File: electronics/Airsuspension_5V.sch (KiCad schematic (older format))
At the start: 5 parts, among them U9 LM2574M-5

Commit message: Some more fottprints added to PCB
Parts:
- C18: footprint (none) -> Capacitors_SMD:c_elec_6.3x7.7
- C19: footprint (none) -> Capacitors_SMD:c_elec_8x10.5
- D12: footprint (none) -> Diodes_SMD:Diode-SMA_Handsoldering
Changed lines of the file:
@@
 F 0 "D12" H 6300 3100 50  0000 C CNN
 F 1 "SS110" H 6300 2900 50  0000 C CNN
-F 2 "" H 6300 3000 60  0001 C CNN
+F 2 "Diodes_SMD:Diode-SMA_Handsoldering" H 6300 3000 60  0001 C CNN
 F 3 "http://www.farnell.com/datasheets/1662144.pdf" H 6300 3000 60  0001 C CNN
 F 4 "4085140" H 6300 3000 60  0001 C CNN "farnell"
@@
 F 0 "C18" H 5950 4000 50  0000 L CNN
 F 1 "47uF lowESR" H 5950 3800 50  0000 L CNN
-F 2 "" H 5938 3750 30  0001 C CNN
+F 2 "Capacitors_SMD:c_elec_6.3x7.7" H 5938 3750 30  0001 C CNN
 F 3 "http://www.farnell.com/datasheets/1679509.pdf" H 5900 3900 60  0001 C CNN
 F 4 "EEETQV470XAP" H 5900 3900 60  0001 C CNN "name"
@@
 F 0 "C19" H 7300 3100 50  0000 L CNN
 F 1 "470uF low esr" H 7000 2900 50  0000 L CNN
-F 2 "" H 7288 2850 30  0001 C CNN
+F 2 "Capacitors_SMD:c_elec_8x10.5" H 7288 2850 30  0001 C CNN
 F 3 "http://www.farnell.com/datasheets/1790597.pdf" H 7250 3000 60  0001 C CNN
 F 4 "EEEFT1E471AP" H 7250 3000 60  0001 C CNN "name"

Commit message: Some more footprints and beginning PCB work
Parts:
- L1: footprint (none) -> kicad_lib:Inductor_MSS1260
- U9: footprint (none) -> kicad_lib:SOIC14_W
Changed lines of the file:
@@
 F 0 "U9" H 5100 3300 60  0000 C CNN
 F 1 "LM2574M-5" H 5100 2500 60  0000 C CNN
-F 2 "" H 5050 2800 60  0001 C CNN
+F 2 "kicad_lib:SOIC14_W" H 5050 2800 60  0001 C CNN
 F 3 "http://www.farnell.com/datasheets/1896110.pdf" H 5050 2800 60  0001 C CNN
 F 4 "9489908" H 5100 2900 60  0001 C CNN "farnell"
@@
 F 0 "L1" V 6550 2800 50  0000 C CNN
 F 1 "470uH" V 6700 2800 50  0000 C CNN
-F 2 "" H 6600 2800 60  0001 C CNN
+F 2 "kicad_lib:Inductor_MSS1260" H 6600 2800 60  0001 C CNN
 F 3 "http://www.farnell.com/datasheets/1681951.pdf" H 6600 2800 60  0001 C CNN
 F 4 "MSS1260-474KLD" V 6600 2800 60  0001 C CNN "name"

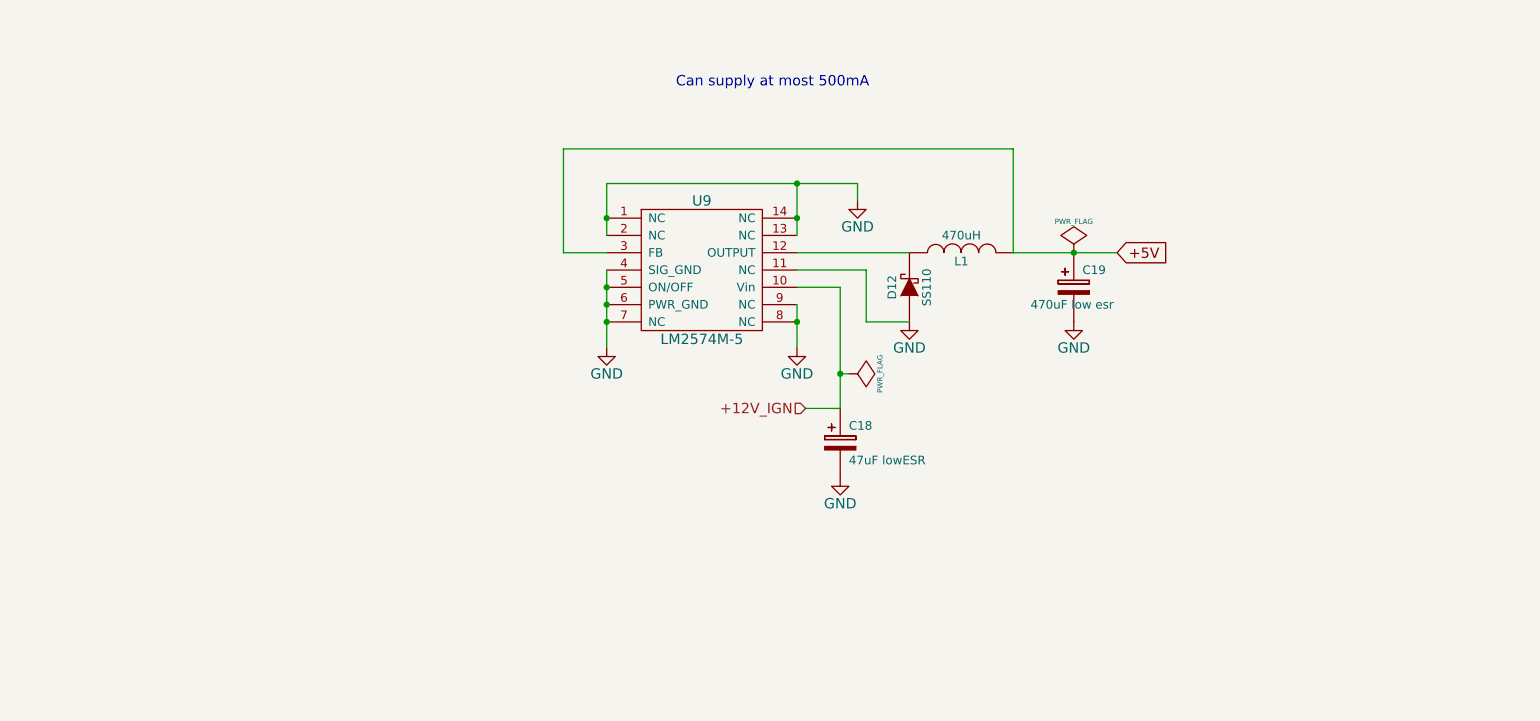
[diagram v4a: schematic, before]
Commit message: Changed to a more stable powersupply (3Amps 5V and separate 3.3v) + some few cleanups due to updated kicad
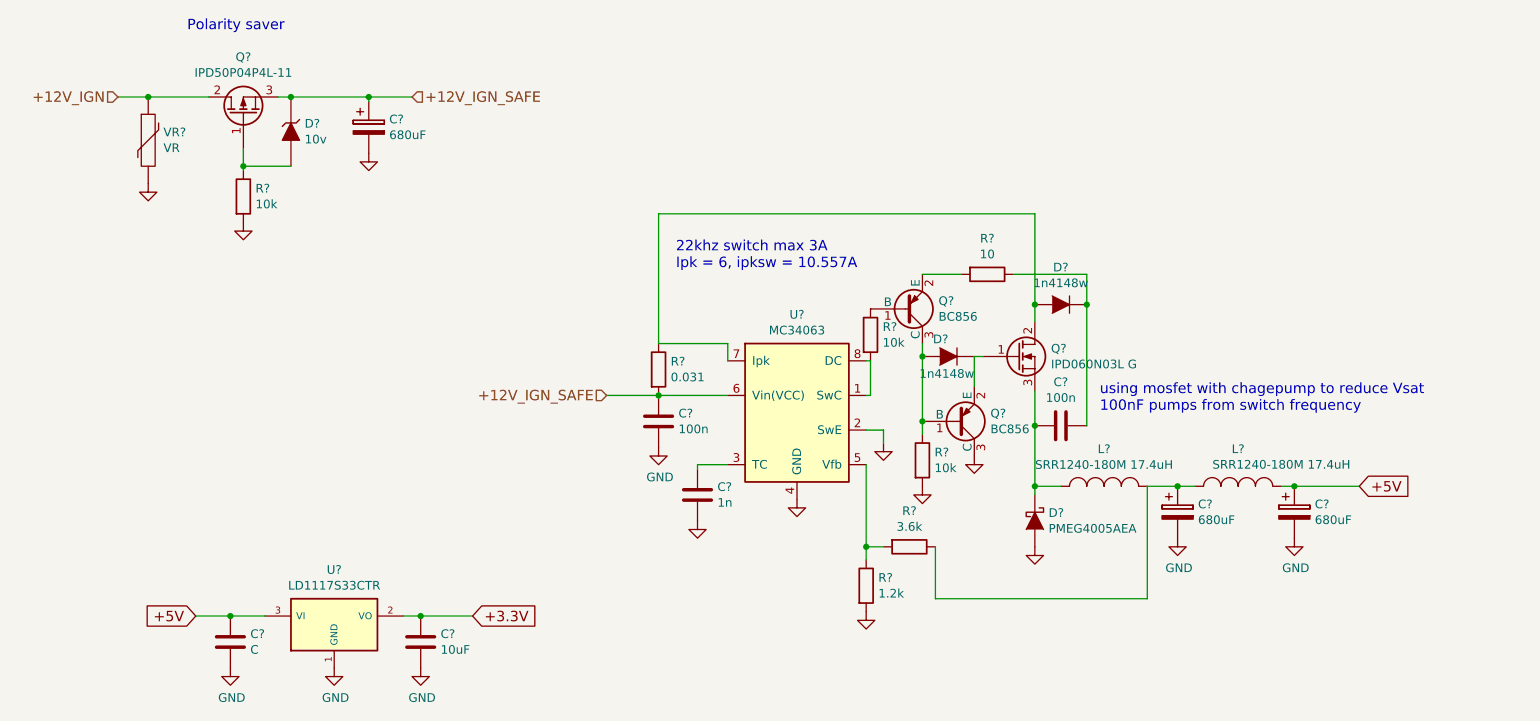
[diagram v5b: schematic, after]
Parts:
- removed C18: 47uF lowESR, Capacitors_SMD:c_elec_6.3x7.7, symbol CP2
- removed C19: 470uF low esr, Capacitors_SMD:c_elec_8x10.5, symbol CP2
- removed D12: SS110, Diodes_SMD:Diode-SMA_Handsoldering, symbol DIODESCH
- removed L1: 470uH, kicad_lib:Inductor_MSS1260, symbol INDUCTOR
- removed U9: LM2574M-5, kicad_lib:SOIC14_W, symbol LM2574
- added C? (x2): 100n, Capacitors_SMD:C_0805_HandSoldering, symbol C
- added C?: 1n, Capacitors_SMD:C_0805_HandSoldering, symbol C
- added C? (x3): 680uF, Capacitors_SMD:c_elec_10x10.5, symbol CP
- added C?: 10uF, Capacitors_SMD:C_1206_HandSoldering, symbol C
- added C?: C, symbol C
- added D? (x2): 1n4148w, Diodes_SMD:SOD-323, symbol D
- added D?: PMEG4005AEA, Diodes_SMD:SOD-323, symbol D_Schottky
- added D?: 10v, Diodes_SMD:SOD-323, symbol ZENER
- added L? (x2): SRR1240-180M 17.4uH, Inductors_NEOSID:Neosid_Inductor_SM-NE127, symbol INDUCTOR_SMALL
- added Q?: IPD060N03L G, TO_SOT_Packages_SMD:TO-252-2Lead, symbol Q_NMOS_GDS
- added Q?: BC856, TO_SOT_Packages_SMD:SOT-23, symbol BC856
- added Q?: BC856, TO_SOT_Packages_SMD:SOT-323, symbol BC856
- added Q?: IPD50P04P4L-11, TO_SOT_Packages_SMD:TO-252-2Lead, symbol Q_PMOS_GDS
- added R?: 1.2k, Resistors_SMD:R_0805_HandSoldering, symbol R
- added R?: 3.6k, Resistors_SMD:R_0805_HandSoldering, symbol R
- added R?: 0.031, Resistors_SMD:R_1206_HandSoldering, symbol R
- added R? (x3): 10k, Resistors_SMD:R_0805_HandSoldering, symbol R
- added R?: 10, Resistors_SMD:R_0805_HandSoldering, symbol R
- added U?: MC34063, symbol MC34063
- added U?: LD1117S33CTR, TO_SOT_Packages_SMD:SOT-223, symbol LD1117S33CTR
- added VR?: VR, Resistors_SMD:R_1206_HandSoldering, symbol VR
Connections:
- net +12V_IGN: now also Q?.2 (D), VR?.1
- net +5V: now also C?.1, C?.1, L?.2, U?.3 (VI)
- net GND: now also C?.2, C?.2, C?.2, C?.2, C?.2, C?.2, C?.2, D?.2 (A), Q?.3 (C), R?.2, R?.2, R?.2, U?.1 (GND), U?.2 (SwE), U?.4 (GND), VR?.2
- new net: R?.2, U?.1 (SwC), U?.8 (DC)
- new net: C?.1, U?.3 (TC)
- new net: R?.1, R?.2, U?.5 (Vfb)
- new net: D?.2 (A), Q?.2 (D), R?.1, U?.7 (Ipk)
- new net: C?.1, L?.1, L?.2, R?.1
- new net: C?.1, D?.1 (K), R?.1
- new net: C?.2, D?.1 (K), L?.1, Q?.3 (S)
- new net: D?.1 (K), Q?.1 (G), Q?.2 (E)
- new net: D?.2 (A), Q?.1 (B), Q?.3 (C), R?.1
- new net: Q?.2 (E), R?.2
- new net: Q?.1 (B), R?.1
- new net: D?.2 (A), Q?.1 (G), R?.1
- new net +12V_IGN_SAFE: C?.1, C?.1, D?.1 (K), Q?.3 (S), R?.2, U?.6 (Vin(VCC))
- new net +3.3V: C?.1, U?.2 (VO)
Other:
- note added: "22khz switch max 3A \nIpk = 6, ipksw = 10.557A"
- note added: "Polarity saver"
- note added: "using mosfet with chagepump to reduce Vsat\n100nF pumps from switch frequency\n"
- note removed: "Can supply at most 500mA"

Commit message: First placement with a ModICE enclosure
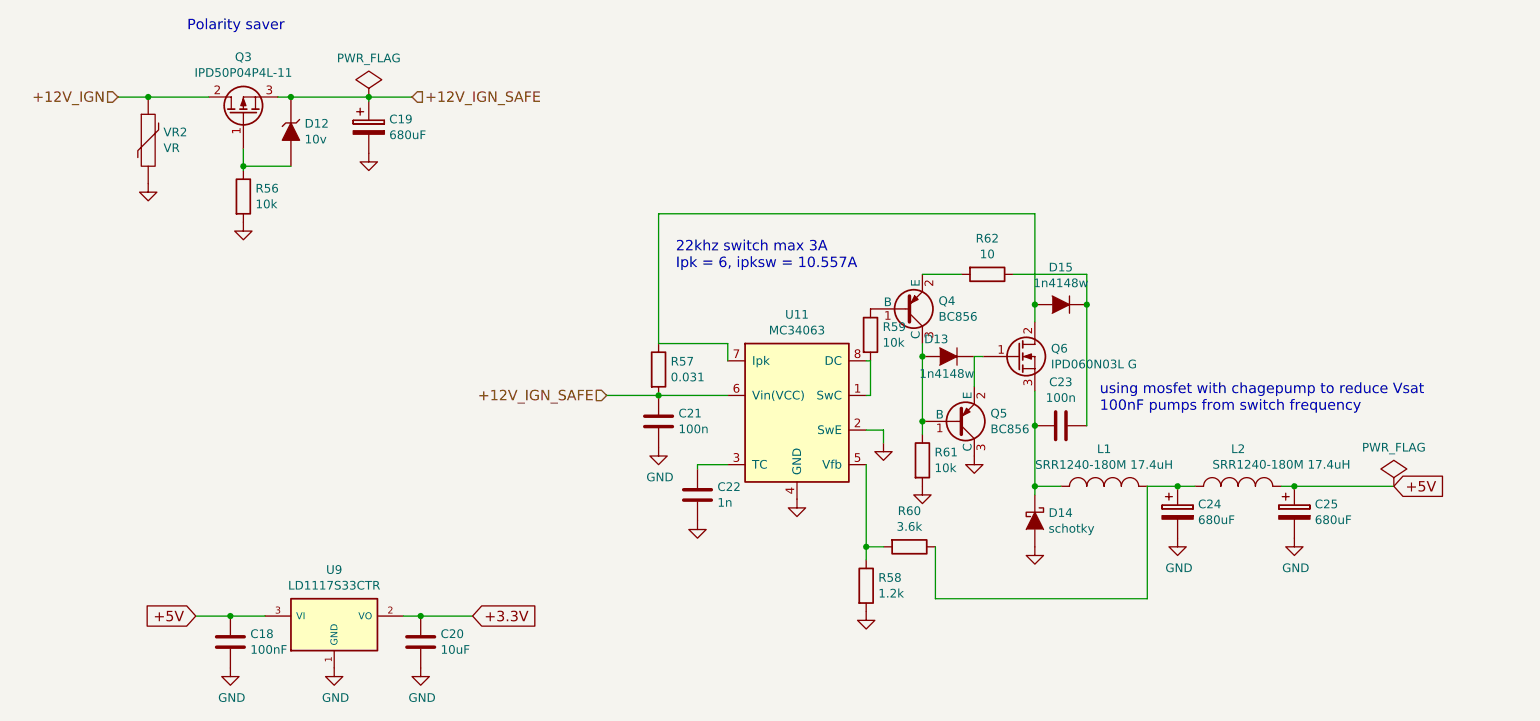
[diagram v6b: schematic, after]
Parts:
- C18: renamed from C?; value C -> 100nF; footprint (none) -> Capacitors_SMD:C_0805_HandSoldering
- D14: renamed from D?; value PMEG4005AEA -> schotky; footprint Diodes_SMD:SOD-323 -> Diodes_SMD:DO-214AB_Handsoldering; farnell 8738025 -> 9557377; part (none) -> MBRS340T3G
- Q4: renamed from Q?; footprint TO_SOT_Packages_SMD:SOT-323 -> TO_SOT_Packages_SMD:SOT-23_Handsoldering
- Q5: renamed from Q?; footprint TO_SOT_Packages_SMD:SOT-23 -> TO_SOT_Packages_SMD:SOT-23_Handsoldering
- U11: renamed from U?; footprint (none) -> Housings_SOIC:SOIC-8_3.9x4.9mm_Pitch1.27mm; farnell (none) -> 1087205; part (none) -> MC34063ABD-TR
- gave numbers to parts that had none: 23

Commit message: Some updates as some parts were not available
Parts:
- C20: farnell 2522130 -> 1463368; part C3216X7R1C106K160AC -> (none)
- R62: farnell 9332421 -> 9332766
- U9: farnell 2253482 -> 1467779
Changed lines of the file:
@@
 F 2 "Resistors_SMD:R_0805_HandSoldering" H 6820 2834 50  0001 L CNN
 F 3 "" H 6750 2925 50  0000 C CNN
-F 4 "9332421" H 6750 2925 60  0001 C CNN "farnell"
+F 4 "9332766" H 6750 2925 60  0001 C CNN "farnell"
 	1    6750 2925
 	0    1    1    0
@@
 F 2 "TO_SOT_Packages_SMD:SOT-223" H 2975 5176 50  0001 C CNN
 F 3 "" H 2975 4950 50  0000 C CNN
-F 4 "2253482" H 2975 4950 60  0001 C CNN "farnell"
+F 4 "1467779" H 2975 4950 60  0001 C CNN "farnell"
 	1    2975 4950
 	1    0    0    -1
@@
 F 2 "Capacitors_SMD:C_1206_HandSoldering" H 3590 4959 50  0001 L CNN
 F 3 "" H 3475 5050 50  0000 C CNN
-F 4 "2522130" H 3475 5050 60  0001 C CNN "farnell"
-F 5 "C3216X7R1C106K160AC" H 3475 5050 60  0001 C CNN "part"
+F 4 "1463368" H 3475 5050 60  0001 C CNN "farnell"
 	1    3475 5050
 	1    0    0    -1
